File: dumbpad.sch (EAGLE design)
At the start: 36 parts

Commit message: diodes...
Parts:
- removed R10, R11, R12, R13, R14, R15, R16, R17, R18, R3, R4, R5, R6, R7, R8, R9: 10k, SparkFun-Resistors:10KOHM-0603-1/10W-1%
- added D1, D10, D11, D12, D13, D14, D15, D16, D2, D3, D4, D5, D6, D7, D8, D9: (no value), adafruit:DIODEDO-1N4148
- R1, R2: device SparkFun-Resistors:10KOHM-0603-1/10W-1% -> SparkFun-Resistors:10KOHM-HORIZ-1/4W-1%
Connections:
- removed net ROW0_S2: R2.1, R3.2, S2.1
- removed net ROW0_S3: R3.1, R4.2, S3.1
- removed net ROW0_S4: R4.1, S4.1
- removed net ROW1_S6: R6.1, R7.2, S6.1
- removed net ROW1_S7: R7.1, R8.2, S7.1
- removed net ROW1_S8: R8.1, S8.1
- removed net ROW2_S10: R10.1, R11.2, S10.1
- removed net ROW2_S11: R11.1, R12.2, S11.1
- removed net ROW2_S12: R12.1, S12.1
- removed net ROW3_S14: R14.1, R15.2, S14.1
- removed net ROW3_S15: R15.1, R16.2, S15.1
- removed net ROW3_S16: R16.1, S16.1
- new net COL0: B1.*6, S1.2, S13.2, S5.2, S9.2
- new net COL1: B1.7, S10.2, S14.2, S2.2, S6.2
- new net COL2: B1.8, S11.2, S15.2, S3.2, S7.2
- new net COL3: B1.*9, S12.2, S16.2, S4.2, S8.2
- new net N$1: D4.A, S4.1
- new net N$11: D16.A, S16.1
- new net N$12: D15.A, S15.1
- new net N$13: D14.A, S14.1
- new net N$14: D13.A, S13.1
- new net N$16: D12.A, S12.1
- new net N$17: D11.A, S11.1
- new net N$18: D10.A, S10.1
- new net N$19: D9.A, S9.1
- new net N$2: D3.A, S3.1
- new net N$3: D2.A, S2.1
- new net N$4: D1.A, S1.1
- new net N$6: D8.A, S8.1
- new net N$7: D7.A, S7.1
- new net N$8: D6.A, S6.1
- new net N$9: D5.A, S5.1
- net ENCODER_L0: now also R1.1; no longer R17.1
- net ENCODER_L1: now also R2.1; no longer R18.1
- net GND: no longer S1.2, S10.2, S11.2, S12.2, S13.2, S14.2, S15.2, S16.2, S2.2, S3.2, S4.2, S5.2, S6.2, S7.2, S8.2, S9.2
- net ROW0: now also D1.C, D2.C, D3.C, D4.C; no longer R1.1, R2.2, S1.1
- net ROW1: now also D5.C, D6.C, D7.C, D8.C; no longer R5.1, R6.2, S5.1
- net ROW2: now also D10.C, D11.C, D12.C, D9.C; no longer R10.2, R9.1, S9.1
- net ROW3: now also D13.C, D14.C, D15.C, D16.C; no longer R13.1, R14.2, S13.1
- net VCC: now also R2.2; no longer R13.2, R17.2, R18.2, R5.2, R9.2
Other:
- moved on the sheet: R1, R2, S10, S11, S12, S14, S15, S16, S2, S3, S4, S6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

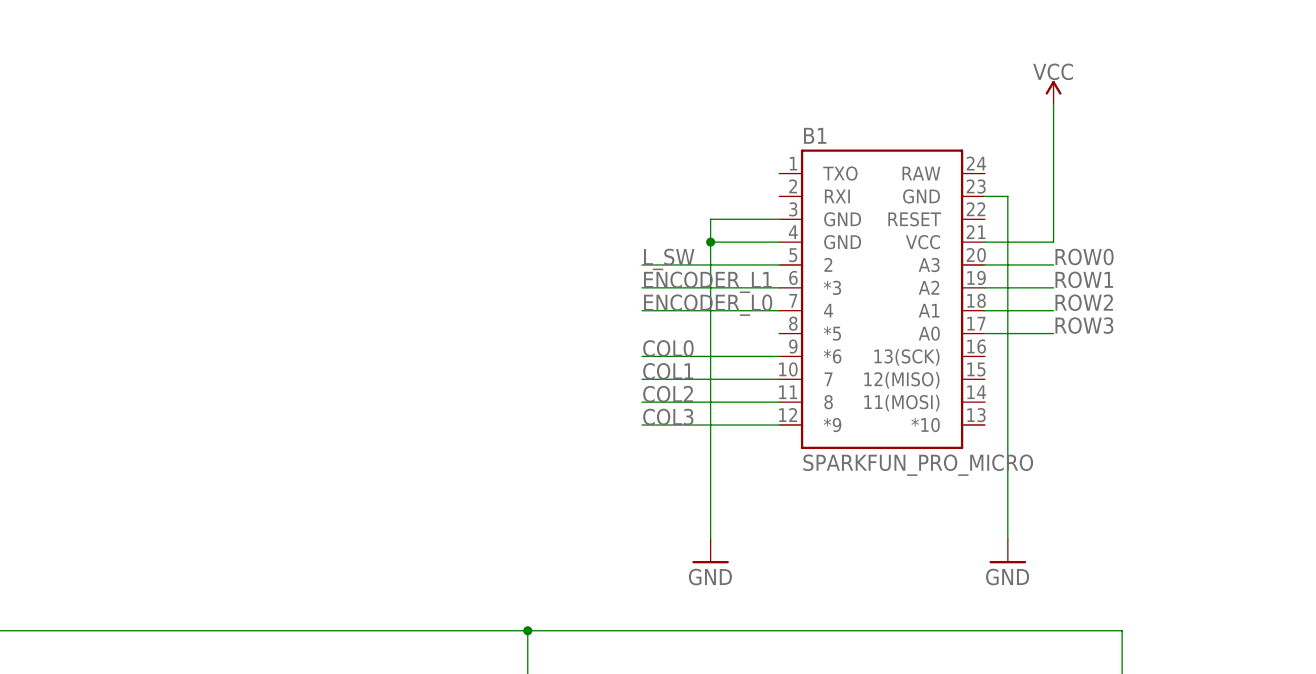
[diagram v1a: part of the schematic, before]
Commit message: added reset button, centered diodes on switches
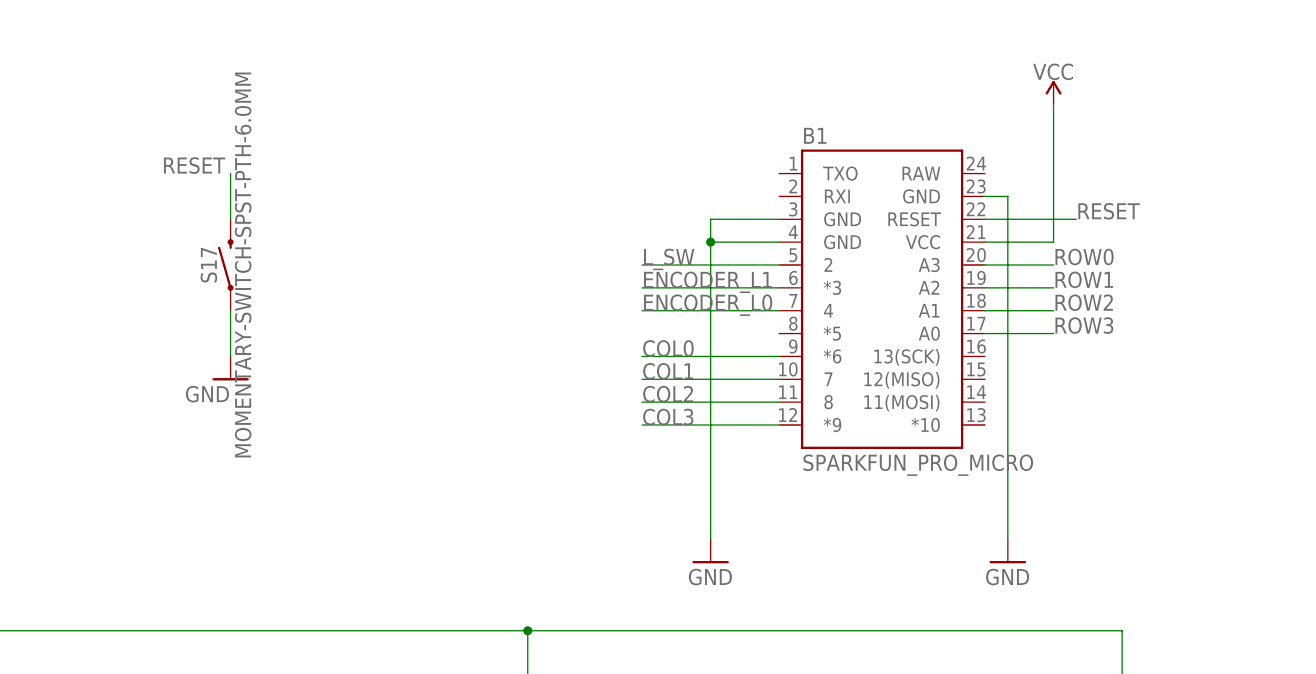
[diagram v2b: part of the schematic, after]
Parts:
- added S17: MOMENTARY-SWITCH-SPST-PTH-6.0MM, SparkFun-Switches:MOMENTARY-SWITCH-SPST-PTH-6.0MM
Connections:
- new net RESET: B1.RESET, S17.2
- net GND: now also S17.1
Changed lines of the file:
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@@
 <part name="R1" library="SparkFun-Resistors" deviceset="10KOHM" device="-HORIZ-1/4W-1%" value="10k"/>
 <part name="R2" library="SparkFun-Resistors" deviceset="10KOHM" device="-HORIZ-1/4W-1%" value="10k"/>
+<part name="S17" library="SparkFun-Switches" deviceset="MOMENTARY-SWITCH-SPST" device="-PTH-6.0MM"/>
+<part name="GND4" library="supply1" library_urn="urn:adsk.eagle:library:371" deviceset="GND" device=""/>
 </parts>
 <sheets>
@@
 <attribute name="VALUE" x="-21.336" y="76.2" size="1.778" layer="96" font="vector" rot="R90" align="top-center"/>
 </instance>
+<instance part="S17" gate="G$1" x="78.74" y="66.04" smashed="yes" rot="R90">
+<attribute name="NAME" x="77.216" y="66.04" size="1.778" layer="95" font="vector" rot="R90" align="bottom-center"/>
+<attribute name="VALUE" x="79.248" y="66.04" size="1.778" layer="96" font="vector" rot="R90" align="top-center"/>
+</instance>
+<instance part="GND4" gate="1" x="78.74" y="53.34" smashed="yes">
+<attribute name="VALUE" x="73.66" y="50.8" size="1.778" layer="96"/>
+</instance>
 </instances>
 <busses>
@@
 <junction x="132.08" y="68.58"/>
 <pinref part="GND3" gate="1" pin="GND"/>
+</segment>
+<segment>
+<pinref part="S17" gate="G$1" pin="1"/>
+<pinref part="GND4" gate="1" pin="GND"/>
+<wire x1="78.74" y1="60.96" x2="78.74" y2="55.88" width="0.1524" layer="91"/>
 </segment>
 </net>
@@
 </segment>
 </net>
+<net name="RESET" class="0">
+<segment>
+<pinref part="B1" gate="G$1" pin="RESET"/>
+<wire x1="162.56" y1="71.12" x2="172.72" y2="71.12" width="0.1524" layer="91"/>
+<label x="172.72" y="71.12" size="1.778" layer="95"/>
+</segment>
+<segment>
+<pinref part="S17" gate="G$1" pin="2"/>
+<wire x1="78.74" y1="71.12" x2="78.74" y2="76.2" width="0.1524" layer="91"/>
+<label x="71.12" y="76.2" size="1.778" layer="95"/>
+</segment>
+</net>

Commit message: minor tweaks, sch as png
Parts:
- added D17: (no value), adafruit:DIODEDO-1N4148
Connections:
- removed net L_SW: B1.2, RE1G$2.2
- new net COL4: B1.*9, S12.2, S16.2, S4.2, S8.2
- new net N$10: D17.A, RE1G$2.2
- net COL0: now also B1.*5, RE1G$2.1; no longer B1.*6, S1.2, S13.2, S5.2, S9.2
- net COL1: now also B1.*6, S1.2, S13.2, S5.2, S9.2; no longer B1.7, S10.2, S14.2, S2.2, S6.2
- net COL2: now also B1.7, S10.2, S14.2, S2.2, S6.2; no longer B1.8, S11.2, S15.2, S3.2, S7.2
- net COL3: now also B1.8, S11.2, S15.2, S3.2, S7.2; no longer B1.*9, S12.2, S16.2, S4.2, S8.2
- net GND: no longer RE1G$2.1
- net ROW3: now also D17.C
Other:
- note added: "Date: July 14, 2019"
- note added: "Design By: github.com/imchipwood"
- note added: "Rev: 0.2"
- note added: "Title: dumbpad"
- moved on the sheet: B1, D1, D10, D11, D12, D13, D14, D15, D16, D2, D3, D4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

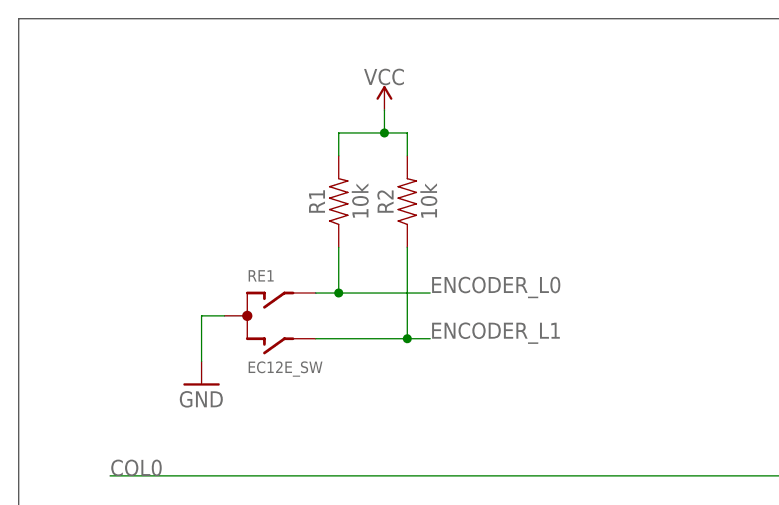
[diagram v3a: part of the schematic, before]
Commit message: removed resistors from rotary encoder, updated readme
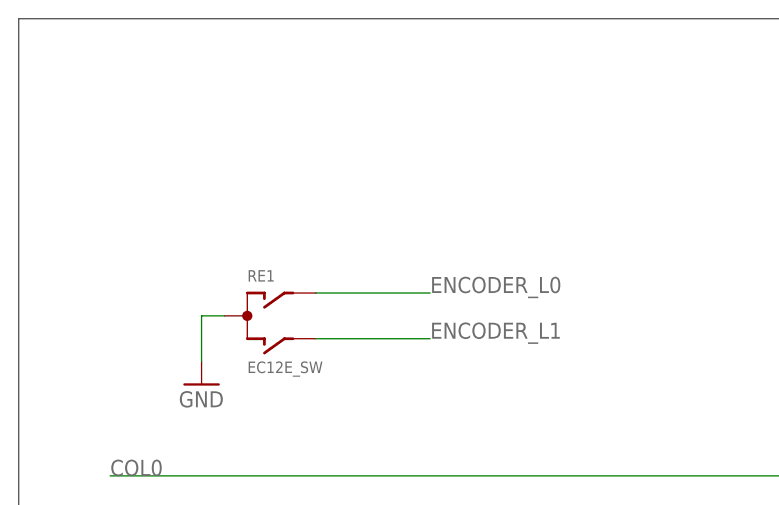
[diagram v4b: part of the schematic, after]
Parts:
- removed R1, R2: 10k, SparkFun-Resistors:10KOHM-HORIZ-1/4W-1%
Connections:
- net ENCODER_L0: no longer R1.1
- net ENCODER_L1: no longer R2.1
- net VCC: no longer R1.2, R2.2
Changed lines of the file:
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@@
 <part name="S16" library="SparkFun-Switches" deviceset="MOMENTARY-SWITCH-SPST-LED" device="-PTH-CHERRY"/>
 <part name="GND3" library="supply1" library_urn="urn:adsk.eagle:library:371" deviceset="GND" device=""/>
-<part name="SUPPLY1" library="SparkFun-PowerSymbols" deviceset="VCC" device=""/>
 <part name="SUPPLY2" library="SparkFun-PowerSymbols" deviceset="VCC" device=""/>
 <part name="D1" library="adafruit" deviceset="DIODE" device="DO-1N4148"/>
@@
 <part name="D15" library="adafruit" deviceset="DIODE" device="DO-1N4148"/>
 <part name="D16" library="adafruit" deviceset="DIODE" device="DO-1N4148"/>
-<part name="R1" library="SparkFun-Resistors" deviceset="10KOHM" device="-HORIZ-1/4W-1%" value="10k"/>
-<part name="R2" library="SparkFun-Resistors" deviceset="10KOHM" device="-HORIZ-1/4W-1%" value="10k"/>
 <part name="S17" library="SparkFun-Switches" deviceset="MOMENTARY-SWITCH-SPST" device="-PTH-6.0MM"/>
 <part name="GND4" library="supply1" library_urn="urn:adsk.eagle:library:371" deviceset="GND" device=""/>
@@
 <attribute name="VALUE" x="261.62" y="106.68" size="1.778" layer="96"/>
 </instance>
-<instance part="SUPPLY1" gate="G$1" x="40.64" y="162.56" smashed="yes">
-<attribute name="VALUE" x="40.64" y="165.354" size="1.778" layer="96" align="bottom-center"/>
-</instance>
 <instance part="SUPPLY2" gate="G$1" x="302.26" y="160.02" smashed="yes">
 <attribute name="VALUE" x="302.26" y="162.814" size="1.778" layer="96" align="bottom-center"/>
@@
 <attribute name="NAME" x="226.06" y="15.24" size="1.27" layer="95" rot="R180"/>
 <attribute name="VALUE" x="226.06" y="21.59" size="1.27" layer="96" rot="R180"/>
-</instance>
-<instance part="R1" gate="G$1" x="35.56" y="152.4" smashed="yes" rot="R90">
-<attribute name="NAME" x="34.036" y="152.4" size="1.778" layer="95" font="vector" rot="R90" align="bottom-center"/>
-<attribute name="VALUE" x="37.084" y="152.4" size="1.778" layer="96" font="vector" rot="R90" align="top-center"/>
-</instance>
-<instance part="R2" gate="G$1" x="43.18" y="152.4" smashed="yes" rot="R90">
-<attribute name="NAME" x="41.656" y="152.4" size="1.778" layer="95" font="vector" rot="R90" align="bottom-center"/>
-<attribute name="VALUE" x="44.704" y="152.4" size="1.778" layer="96" font="vector" rot="R90" align="top-center"/>
 </instance>
 <instance part="S17" gate="G$1" x="294.64" y="73.66" smashed="yes" rot="R90">
@@
 <segment>
 <pinref part="RE1" gate="G$1" pin="A"/>
-<wire x1="33.02" y1="142.24" x2="35.56" y2="142.24" width="0.1524" layer="91"/>
-<wire x1="35.56" y1="142.24" x2="45.72" y2="142.24" width="0.1524" layer="91"/>
-<wire x1="35.56" y1="142.24" x2="35.56" y2="147.32" width="0.1524" layer="91"/>
-<junction x="35.56" y="142.24"/>
+<wire x1="33.02" y1="142.24" x2="45.72" y2="142.24" width="0.1524" layer="91"/>
 <label x="45.72" y="142.24" size="1.778" layer="95"/>
-<pinref part="R1" gate="G$1" pin="1"/>
 </segment>
 <segment>
@@
 <segment>
 <pinref part="RE1" gate="G$1" pin="B"/>
-<wire x1="33.02" y1="137.16" x2="43.18" y2="137.16" width="0.1524" layer="91"/>
-<wire x1="43.18" y1="137.16" x2="43.18" y2="147.32" width="0.1524" layer="91"/>
-<wire x1="43.18" y1="137.16" x2="45.72" y2="137.16" width="0.1524" layer="91"/>
-<junction x="43.18" y="137.16"/>
+<wire x1="33.02" y1="137.16" x2="45.72" y2="137.16" width="0.1524" layer="91"/>
 <label x="45.72" y="137.16" size="1.778" layer="95"/>
-<pinref part="R2" gate="G$1" pin="1"/>
 </segment>
 </net>
@@
 <net name="VCC" class="0">
 <segment>
-<wire x1="35.56" y1="157.48" x2="35.56" y2="160.02" width="0.1524" layer="91"/>
-<wire x1="35.56" y1="160.02" x2="40.64" y2="160.02" width="0.1524" layer="91"/>
-<wire x1="40.64" y1="160.02" x2="43.18" y2="160.02" width="0.1524" layer="91"/>
-<wire x1="43.18" y1="160.02" x2="43.18" y2="157.48" width="0.1524" layer="91"/>
-<wire x1="40.64" y1="160.02" x2="40.64" y2="162.56" width="0.1524" layer="91"/>
-<junction x="40.64" y="160.02"/>
-<pinref part="SUPPLY1" gate="G$1" pin="VCC"/>
-<pinref part="R1" gate="G$1" pin="2"/>
-<pinref part="R2" gate="G$1" pin="2"/>
-</segment>
-<segment>
 <pinref part="B1" gate="G$1" pin="VCC"/>

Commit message: moved all components to top, rerouted
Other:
- note added: "Date: July 28, 2019"
- note added: "Rev: 0.4"
- note removed: "Date: July 14, 2019"
- note removed: "Rev: 0.2"
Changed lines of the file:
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@@
 <wire x1="0" y1="172.72" x2="0" y2="0" width="0.1524" layer="97"/>
 <text x="307.34" y="2.54" size="1.778" layer="97">Rev:
-0.2</text>
+0.4</text>
 <text x="279.4" y="2.54" size="1.778" layer="97">Date:
-July 14, 2019</text>
+July 28, 2019</text>
 <text x="279.4" y="10.16" size="1.778" layer="97">Design By:
 github.com/imchipwood</text>

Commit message: who doesn't like LEDs
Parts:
- added D18, D19: (no value), SparkFun-LED:LED3MM
- added R1, R2: 330, SparkFun-Resistors:330OHM-HORIZ-1/10W-5%
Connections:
- new net LED0: B1.13(SCK), R1.2
- new net LED1: B1.12(MISO), R2.2
- new net N$15: D19.A, R2.1
- new net N$5: D18.A, R1.1
- net GND: now also D18.C, D19.C
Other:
- note added: "Rev: 0.5"
- note removed: "Rev: 0.4"
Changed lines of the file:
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@@
 <layer number="115" name="ReferenceISLANDS" color="7" fill="1" visible="no" active="no"/>
 <layer number="116" name="Patch_BOT" color="9" fill="4" visible="no" active="no"/>
+<layer number="117" name="PM_Ref" color="26" fill="1" visible="yes" active="yes"/>
 <layer number="118" name="Rect_Pads" color="7" fill="1" visible="no" active="no"/>
+<layer number="119" name="PF_Ref" color="31" fill="1" visible="yes" active="yes"/>
+<layer number="120" name="WFL_Ref" color="25" fill="1" visible="yes" active="yes"/>
 <layer number="121" name="_tsilk" color="7" fill="1" visible="no" active="no"/>
 <layer number="122" name="_bsilk" color="7" fill="1" visible="no" active="no"/>
@@
 <part name="GND4" library="supply1" library_urn="urn:adsk.eagle:library:371" deviceset="GND" device=""/>
 <part name="D17" library="adafruit" deviceset="DIODE" device="DO-1N4148"/>
+<part name="D18" library="SparkFun-LED" deviceset="LED" device="3MM"/>
+<part name="D19" library="SparkFun-LED" deviceset="LED" device="3MM"/>
+<part name="R1" library="SparkFun-Resistors" deviceset="330OHM" device="-HORIZ-1/10W-5%" value="330"/>
+<part name="R2" library="SparkFun-Resistors" deviceset="330OHM" device="-HORIZ-1/10W-5%" value="330"/>
+<part name="GND2" library="supply1" library_urn="urn:adsk.eagle:library:371" deviceset="GND" device=""/>
 </parts>
 <sheets>
@@
 <wire x1="0" y1="172.72" x2="0" y2="0" width="0.1524" layer="97"/>
 <text x="307.34" y="2.54" size="1.778" layer="97">Rev:
-0.4</text>
+0.5</text>
 <text x="279.4" y="2.54" size="1.778" layer="97">Date:
 July 28, 2019</text>
@@
 <attribute name="VALUE" x="226.06" y="133.35" size="1.27" layer="96" rot="R180"/>
 </instance>
+<instance part="D18" gate="D1" x="160.02" y="139.7" smashed="yes">
+<attribute name="NAME" x="156.591" y="135.128" size="1.778" layer="95" font="vector" rot="R90"/>
+<attribute name="VALUE" x="161.925" y="135.128" size="1.778" layer="96" font="vector" rot="R90" align="top-left"/>
+</instance>
+<instance part="D19" gate="D1" x="170.18" y="139.7" smashed="yes">
+<attribute name="NAME" x="166.751" y="135.128" size="1.778" layer="95" font="vector" rot="R90"/>
+<attribute name="VALUE" x="172.085" y="135.128" size="1.778" layer="96" font="vector" rot="R90" align="top-left"/>
+</instance>
+<instance part="R1" gate="G$1" x="160.02" y="152.4" smashed="yes" rot="R90">
+<attribute name="NAME" x="158.496" y="152.4" size="1.778" layer="95" font="vector" rot="R90" align="bottom-center"/>
+<attribute name="VALUE" x="161.544" y="152.4" size="1.778" layer="96" font="vector" rot="R90" align="top-center"/>
+</instance>
+<instance part="R2" gate="G$1" x="170.18" y="152.4" smashed="yes" rot="R90">
+<attribute name="NAME" x="168.656" y="152.4" size="1.778" layer="95" font="vector" rot="R90" align="bottom-center"/>
+<attribute name="VALUE" x="171.704" y="152.4" size="1.778" layer="96" font="vector" rot="R90" align="top-center"/>
+</instance>
+<instance part="GND2" gate="1" x="165.1" y="127" smashed="yes">
+<attribute name="VALUE" x="162.56" y="124.46" size="1.778" layer="96"/>
+</instance>
 </instances>
 <busses>
@@
 <pinref part="GND4" gate="1" pin="GND"/>
 <wire x1="294.64" y1="68.58" x2="294.64" y2="63.5" width="0.1524" layer="91"/>
+</segment>
+<segment>
+<pinref part="D18" gate="D1" pin="C"/>
+<wire x1="160.02" y1="134.62" x2="160.02" y2="132.08" width="0.1524" layer="91"/>
+<wire x1="160.02" y1="132.08" x2="165.1" y2="132.08" width="0.1524" layer="91"/>
+<pinref part="GND2" gate="1" pin="GND"/>
+<wire x1="165.1" y1="132.08" x2="165.1" y2="129.54" width="0.1524" layer="91"/>
+<wire x1="165.1" y1="132.08" x2="170.18" y2="132.08" width="0.1524" layer="91"/>
+<junction x="165.1" y="132.08"/>
+<pinref part="D19" gate="D1" pin="C"/>
+<wire x1="170.18" y1="132.08" x2="170.18" y2="134.62" width="0.1524" layer="91"/>
 </segment>
 </net>
@@
 </segment>
 </net>
+<net name="N$5" class="0">
+<segment>
+<pinref part="D18" gate="D1" pin="A"/>
+<pinref part="R1" gate="G$1" pin="1"/>
+<wire x1="160.02" y1="142.24" x2="160.02" y2="147.32" width="0.1524" layer="91"/>
+</segment>
+</net>
+<net name="N$15" class="0">
+<segment>
+<pinref part="R2" gate="G$1" pin="1"/>
+<pinref part="D19" gate="D1" pin="A"/>
+<wire x1="170.18" y1="147.32" x2="170.18" y2="142.24" width="0.1524" layer="91"/>
+</segment>
+</net>
+<net name="LED0" class="0">
+<segment>
+<pinref part="R1" gate="G$1" pin="2"/>
+<wire x1="160.02" y1="157.48" x2="160.02" y2="160.02" width="0.1524" layer="91"/>
+<label x="160.02" y="160.02" size="1.778" layer="95"/>
+</segment>
+<segment>
+<pinref part="B1" gate="G$1" pin="13(SCK)"/>
+<wire x1="294.64" y1="132.08" x2="302.26" y2="132.08" width="0.1524" layer="91"/>
+<label x="302.26" y="132.08" size="1.778" layer="95"/>
+</segment>
+</net>
+<net name="LED1" class="0">
+<segment>
+<pinref part="R2" gate="G$1" pin="2"/>
+<wire x1="170.18" y1="157.48" x2="170.18" y2="160.02" width="0.1524" layer="91"/>
+<label x="170.18" y="160.02" size="1.778" layer="95"/>
+</segment>
+<segment>
+<pinref part="B1" gate="G$1" pin="12(MISO)"/>
+<wire x1="294.64" y1="129.54" x2="302.26" y2="129.54" width="0.1524" layer="91"/>
+<label x="302.26" y="129.54" size="1.778" layer="95"/>
+</segment>
+</net>

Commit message: final touches to v0.5
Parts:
- removed S17: MOMENTARY-SWITCH-SPST-PTH-6.0MM, SparkFun-Switches:MOMENTARY-SWITCH-SPST-PTH-6.0MM
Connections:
- net GND: no longer S17.1
- net RESET: no longer S17.2
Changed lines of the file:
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@@
 <part name="D15" library="adafruit" deviceset="DIODE" device="DO-1N4148"/>
 <part name="D16" library="adafruit" deviceset="DIODE" device="DO-1N4148"/>
-<part name="S17" library="SparkFun-Switches" deviceset="MOMENTARY-SWITCH-SPST" device="-PTH-6.0MM"/>
-<part name="GND4" library="supply1" library_urn="urn:adsk.eagle:library:371" deviceset="GND" device=""/>
 <part name="D17" library="adafruit" deviceset="DIODE" device="DO-1N4148"/>
 <part name="D18" library="SparkFun-LED" deviceset="LED" device="3MM"/>
@@
 <attribute name="VALUE" x="226.06" y="21.59" size="1.27" layer="96" rot="R180"/>
 </instance>
-<instance part="S17" gate="G$1" x="294.64" y="73.66" smashed="yes" rot="R90">
-<attribute name="NAME" x="293.116" y="73.66" size="1.778" layer="95" font="vector" rot="R90" align="bottom-center"/>
-<attribute name="VALUE" x="295.148" y="73.66" size="1.778" layer="96" font="vector" rot="R90" align="top-center"/>
-</instance>
-<instance part="GND4" gate="1" x="294.64" y="60.96" smashed="yes">
-<attribute name="VALUE" x="289.56" y="58.42" size="1.778" layer="96"/>
-</instance>
 <instance part="D17" gate="G$1" x="223.52" y="129.54" smashed="yes" rot="R180">
 <attribute name="NAME" x="226.06" y="127" size="1.27" layer="95" rot="R180"/>
@@
 <junction x="264.16" y="144.78"/>
 <pinref part="GND3" gate="1" pin="GND"/>
-</segment>
-<segment>
-<pinref part="S17" gate="G$1" pin="1"/>
-<pinref part="GND4" gate="1" pin="GND"/>
-<wire x1="294.64" y1="68.58" x2="294.64" y2="63.5" width="0.1524" layer="91"/>
 </segment>
 <segment>
@@
 <label x="304.8" y="147.32" size="1.778" layer="95"/>
 </segment>
-<segment>
-<pinref part="S17" gate="G$1" pin="2"/>
-<wire x1="294.64" y1="78.74" x2="294.64" y2="83.82" width="0.1524" layer="91"/>
-<label x="287.02" y="83.82" size="1.778" layer="95"/>
-</segment>
-</net>
+</net>
